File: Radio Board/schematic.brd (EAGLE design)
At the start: 55 x 70.2 mm, 8 parts, among them J1 132134RP

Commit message: added a 100uF cap
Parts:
- added C3: 08054W107MAT2A, 08054W107MAT2A:CAPC2012X94N
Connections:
- net 3V3.2: now also C3.2
- net GND: now also C3.1
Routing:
- net 3V3.2: track 36.2 -> 37.5 mm
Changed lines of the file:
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@@
 <attribute name="VALUE" x="11.049" y="13.081" size="1.27" layer="27" align="center"/>
+</element>
+<element name="C3" library="08054W107MAT2A" package="CAPC2012X94N" value="08054W107MAT2A" x="40.64" y="40.64" smashed="yes" rot="R180">
+<attribute name="DESCRIPTION" value="Multilayer Ceramic Capacitors MLCC - SMD/SMT 4V 100uF X6S 805 20%" x="40.64" y="40.64" size="1.778" layer="27" rot="R180" display="off"/>
+<attribute name="HEIGHT" value="0.94mm" x="40.64" y="40.64" size="1.778" layer="27" rot="R180" display="off"/>
+<attribute name="MANUFACTURER_NAME" value="Kyocera AVX" x="40.64" y="40.64" size="1.778" layer="27" rot="R180" display="off"/>
+<attribute name="MANUFACTURER_PART_NUMBER" value="08054W107MAT2A" x="40.64" y="40.64" size="1.778" layer="27" rot="R180" display="off"/>
+<attribute name="MOUSER_PART_NUMBER" value="581-08054W107MAT2A" x="40.64" y="40.64" size="1.778" layer="27" rot="R180" display="off"/>
+<attribute name="MOUSER_PRICE-STOCK" value="https://www.mouser.co.uk/ProductDetail/KYOCERA-AVX/08054W107MAT2A?qs=Znm5pLBrcAJdyP%2Fr3h4OXQ%3D%3D" x="40.64" y="40.64" size="1.778" layer="27" rot="R180" display="off"/>
+<attribute name="NAME" x="40.64" y="39" size="1.27" layer="25" rot="R180" align="center"/>
 </element>
 </elements>
@@
 <vertex x="0" y="0"/>
 </polygon>
-<wire x1="28.944" y1="44.207" x2="28.044" y2="44.207" width="0" layer="19" extent="1-1"/>
+<contactref element="C3" pad="1"/>
+<wire x1="35.04" y1="60.335" x2="35.04" y2="64.335" width="0" layer="19" extent="1-1"/>
+<wire x1="40.22" y1="46" x2="35.04" y2="60.335" width="0" layer="19" extent="1-1"/>
+<wire x1="40.22" y1="43.18" x2="40.22" y2="46" width="0" layer="19" extent="1-1"/>
+<wire x1="41.45" y1="40.64" x2="40.22" y2="43.18" width="0" layer="19" extent="1-1"/>
+<wire x1="35.04" y1="40.335" x2="40.22" y2="43.18" width="0" layer="19" extent="1-1"/>
+<wire x1="29.844" y1="42.407" x2="35.04" y2="40.335" width="0" layer="19" extent="1-1"/>
+<wire x1="29.844" y1="43.307" x2="29.844" y2="42.407" width="0" layer="19" extent="1-1"/>
+<wire x1="28.944" y1="43.307" x2="29.844" y2="43.307" width="0" layer="19" extent="1-1"/>
+<wire x1="28.044" y1="43.307" x2="28.944" y2="43.307" width="0" layer="19" extent="1-1"/>
+<wire x1="28.944" y1="44.207" x2="28.944" y2="43.307" width="0" layer="19" extent="1-1"/>
+<wire x1="28.044" y1="44.207" x2="28.044" y2="43.307" width="0" layer="19" extent="1-1"/>
 <wire x1="29.844" y1="44.207" x2="29.844" y2="43.307" width="0" layer="19" extent="1-1"/>
-<wire x1="29.844" y1="42.407" x2="29.844" y2="43.307" width="0" layer="19" extent="1-1"/>
-<wire x1="28.044" y1="42.407" x2="28.944" y2="42.407" width="0" layer="19" extent="1-1"/>
-<wire x1="35.04" y1="40.335" x2="29.844" y2="42.407" width="0" layer="19" extent="1-1"/>
+<wire x1="28.044" y1="42.407" x2="28.044" y2="43.307" width="0" layer="19" extent="1-1"/>
+<wire x1="28.944" y1="42.407" x2="29.844" y2="42.407" width="0" layer="19" extent="1-1"/>
+<wire x1="42" y1="25.32" x2="41.45" y2="40.64" width="0" layer="19" extent="1-1"/>
+<wire x1="48" y1="23.65" x2="42" y2="25.32" width="0" layer="19" extent="1-1"/>
+<wire x1="13.22" y1="38.335" x2="28.044" y2="42.407" width="0" layer="19" extent="1-1"/>
+<wire x1="13.22" y1="64.335" x2="35.04" y2="64.335" width="0" layer="19" extent="1-1"/>
+<wire x1="13.589" y1="9.271" x2="13.22" y2="38.335" width="0" layer="19" extent="1-1"/>
+<wire x1="8.509" y1="9.271" x2="13.589" y2="9.271" width="0" layer="19" extent="1-1"/>
+<wire x1="13.589" y1="4.191" x2="13.589" y2="9.271" width="0" layer="19" extent="1-1"/>
+<wire x1="8.509" y1="4.191" x2="8.509" y2="9.271" width="0" layer="19" extent="1-1"/>
 </signal>
 <signal name="3V3.1">
@@
 <wire x1="38.52" y1="43.18" x2="37.675" y2="42.335" width="0.3048" layer="1"/>
 <wire x1="37.675" y1="42.335" x2="35.04" y2="42.335" width="0.3048" layer="1"/>
-<wire x1="38.52" y1="43.18" x2="38.52" y2="36.41" width="0.3048" layer="1"/>
+<wire x1="38.52" y1="43.18" x2="38.52" y2="40.64" width="0.3048" layer="1"/>
+<wire x1="38.52" y1="40.64" x2="38.52" y2="36.41" width="0.3048" layer="1"/>
 <wire x1="38.52" y1="36.41" x2="39.37" y2="35.56" width="0.3048" layer="1"/>
 <via x="39.37" y="35.56" extent="1-16" drill="0.35"/>
 <wire x1="39.37" y1="35.56" x2="39.37" y2="25.41" width="0.3048" layer="16"/>
 <wire x1="39.37" y1="25.41" x2="42" y2="22.78" width="0.3048" layer="16"/>
+<contactref element="C3" pad="2"/>
+<wire x1="39.83" y1="40.64" x2="38.52" y2="40.64" width="0.3048" layer="1"/>
 </signal>
 <signal name="LIPO">

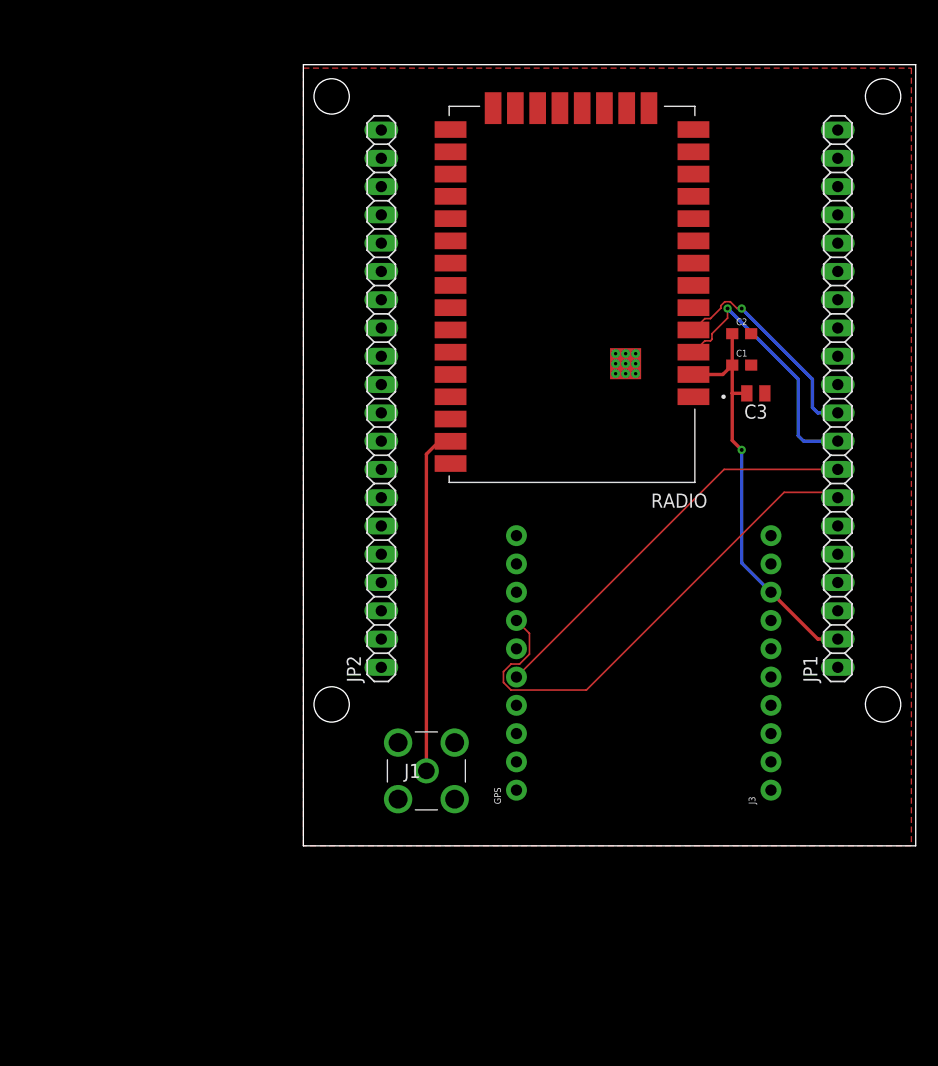
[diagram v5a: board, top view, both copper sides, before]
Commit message: updated radio
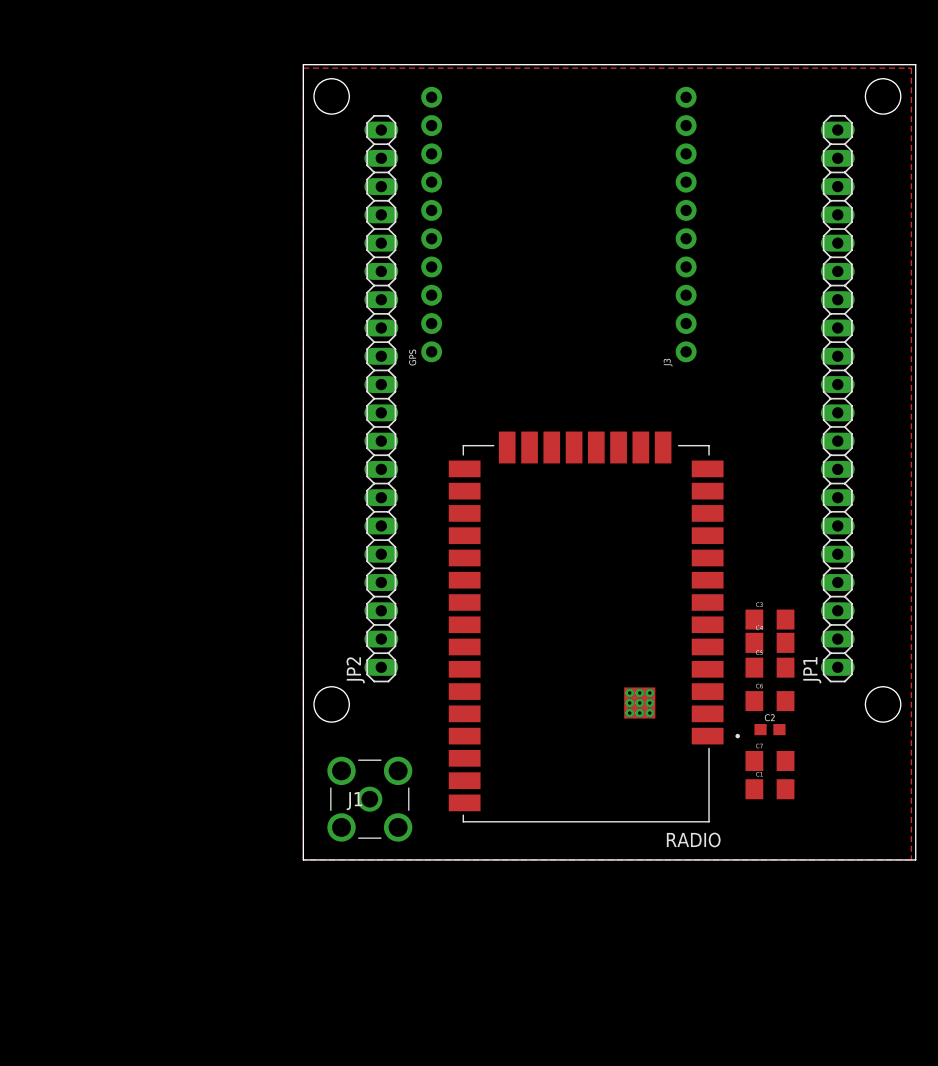
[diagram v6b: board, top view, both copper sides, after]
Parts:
- added C4, C5: 47uF, SparkFun-Retired:1206
- added C6, C7: 100uF, SparkFun-Retired:1206
- C1: device SparkFun-Capacitors:0603 -> SparkFun-Retired:1206
- C3: value 08054W107MAT2A -> 1uF; device 08054W107MAT2A:CAPC2012X94N -> SparkFun-Retired:1206
- moved GPS 40.1 mm to (11.5, 44.4)
- moved J3 40.1 mm to (34.4, 44.4)
- moved C1 38.2 mm to (41.9, 5.08)
- moved C2 35.7 mm to (41.9, 10.4)
- moved RADIO 30.5 mm to (25.4, 19.1)
- moved C3 20.4 mm to (41.9, 20.3), turned to 0 degrees
- moved J1 5.68 mm to (5.97, 4.19)
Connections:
- net 3V3.2: now also C3.1, C4.1, C5.1, C6.1, C7.1; no longer C3.2
- net GND: now also C3.2, C4.2, C5.2, C6.2, C7.2; no longer C3.1
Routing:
- net RX1: track 45.3 -> 0.68 mm
- net 3V3.2: track 37.5 -> 0.00 mm, vias 1 -> 0
- net TX1: track 36.6 -> 0.00 mm
- net RF: track 30.8 -> 0.00 mm
- net RX2: track 24.0 -> 0.68 mm, vias 1 -> 0
- net TX2: track 20.4 -> 0.68 mm, vias 1 -> 0
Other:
- board size 55 x 70.2 mm -> 55 x 71.4 mm

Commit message: Radio Board - Routed traces, missing ground plane
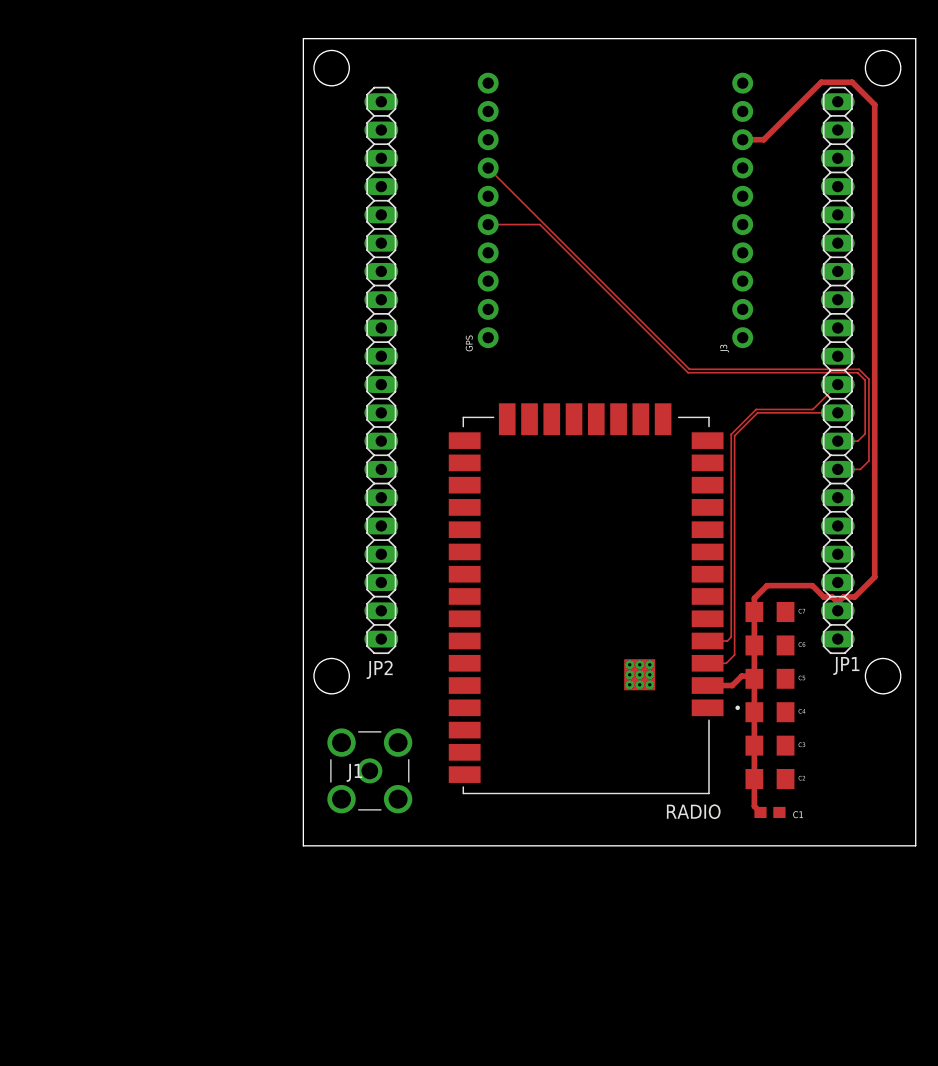
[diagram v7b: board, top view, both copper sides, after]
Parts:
- C1: value 1uF -> 100pF; device SparkFun-Retired:1206 -> SparkFun-Capacitors:0603
- C2: value 100pF -> 1uF; device SparkFun-Capacitors:0603 -> SparkFun-Retired:1206
- moved C7 13.4 mm to (41.9, 21.0)
- moved C3 11.3 mm to (41.9, 9.00)
- moved C4 6.23 mm to (41.9, 12.0)
- moved GPS 5.24 mm to (16.6, 45.6)
- moved J3 5.24 mm to (39.5, 45.6)
- moved C6 5.00 mm to (41.9, 18.0)
- moved C2 4.44 mm to (41.9, 6.00)
- moved JP1 2.54 mm to (48.0, 42.7)
- moved JP2 2.54 mm to (7.00, 42.7)
- moved J1 2.54 mm to (5.97, 6.73)
- moved RADIO 2.54 mm to (25.4, 21.6)
- moved C1 2.08 mm to (41.9, 3.00)
- moved C5 1.00 mm to (41.9, 15.0)
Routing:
- net 3V3.2: track 0.00 -> 111.1 mm
- net RX1: track 0.68 -> 52.5 mm
- net TX1: track 0.00 -> 47.2 mm
- net RX2: track 0.68 -> 32.5 mm
- net TX2: track 0.68 -> 31.9 mm
- removed copper zone on layer 1, net GND
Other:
- board size 55 x 71.4 mm -> 55 x 72.5 mm

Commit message: Planes included, added backups to gitignore
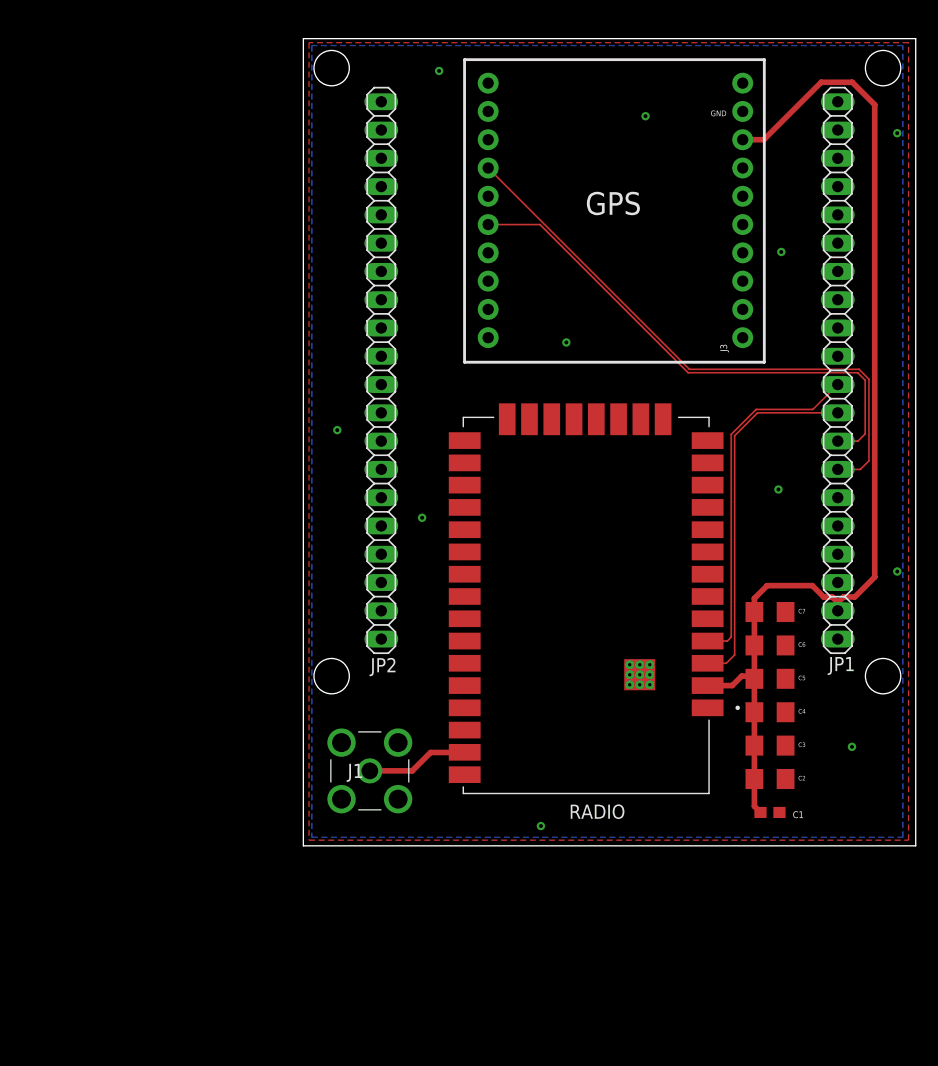
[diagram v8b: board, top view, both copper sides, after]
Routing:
- net RF: track 0.00 -> 9.70 mm
- added copper zone on layer 1, net GND
- added copper zone on layer 16, net GND
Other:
- board text added: "GND"
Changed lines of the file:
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@@
 <dimension x1="55" y1="72.7" x2="0" y2="72.7" x3="27.5" y3="77.47" textsize="1.778" layer="1"/>
 <dimension x1="55" y1="0" x2="55" y2="72.5" x3="63.5" y3="36.25" textsize="1.778" layer="1"/>
+<text x="36.576" y="65.532" size="0.508" layer="21">GND</text>
+<wire x1="14.478" y1="70.612" x2="14.478" y2="43.434" width="0.254" layer="21"/>
+<wire x1="14.478" y1="43.434" x2="41.402" y2="43.434" width="0.254" layer="21"/>
+<wire x1="41.402" y1="43.434" x2="41.402" y2="70.612" width="0.254" layer="21"/>
+<wire x1="41.402" y1="70.612" x2="14.478" y2="70.612" width="0.254" layer="21"/>
 </plain>
 <attributes>
@@
 <elements>
 <element name="JP1" library="adafruit" library_urn="urn:adsk.eagle:library:420" package="1X20" package3d_urn="urn:adsk.eagle:package:6240777/1" value="" x="48" y="42.7" smashed="yes" rot="R90">
-<attribute name="NAME" x="50.0862" y="16.9612" size="1.27" layer="25" ratio="10" rot="R180"/>
+<attribute name="NAME" x="49.5782" y="16.9612" size="1.27" layer="25" ratio="10" rot="R180"/>
 <attribute name="VALUE" x="51.175" y="17.3" size="1.27" layer="27" rot="R90"/>
 </element>
 <element name="JP2" library="adafruit" library_urn="urn:adsk.eagle:library:420" package="1X20" package3d_urn="urn:adsk.eagle:package:6240777/1" value="" x="7" y="42.7" smashed="yes" rot="R90">
-<attribute name="NAME" x="8.1762" y="16.6012" size="1.27" layer="25" ratio="10" rot="R180"/>
+<attribute name="NAME" x="8.4302" y="16.8552" size="1.27" layer="25" ratio="10" rot="R180"/>
 <attribute name="VALUE" x="10.175" y="17.3" size="1.27" layer="27" rot="R90"/>
 </element>
 <element name="GPS" library="SparkFun-Connectors" package="1X10_NO_SILK" value="" x="16.6" y="45.64" smashed="yes" rot="R90">
-<attribute name="NAME" x="15.203" y="44.37" size="0.6096" layer="25" font="vector" ratio="20" rot="R90"/>
+<attribute name="NAME" x="25.32" y="56.679" size="2.032" layer="25" ratio="20"/>
 <attribute name="VALUE" x="18.632" y="44.37" size="0.6096" layer="27" font="vector" ratio="20" rot="R90"/>
 </element>
@@
 <attribute name="MF" value="Digi International" x="52.07" y="-19.05" size="1.778" layer="27" rot="R180" display="off"/>
 <attribute name="MP" value="XBP9X-DMRS-001" x="52.07" y="-19.05" size="1.778" layer="27" rot="R180" display="off"/>
-<attribute name="NAME" x="37.56" y="3.7" size="1.27" layer="25" rot="R180"/>
+<attribute name="NAME" x="28.924" y="3.7" size="1.27" layer="25" rot="R180"/>
 <attribute name="PACKAGE" value="Module Digi International" x="52.07" y="-19.05" size="1.778" layer="27" rot="R180" display="off"/>
 <attribute name="PRICE" value="None" x="52.07" y="-19.05" size="1.778" layer="27" rot="R180" display="off"/>
 <attribute name="PURCHASE-URL" value="https://pricing.snapeda.com/search/part/XBP9X-DMRS-001/?ref=eda" x="52.07" y="-19.05" size="1.778" layer="27" rot="R180" display="off"/>
-<attribute name="VALUE" x="37.81" y="40.4" size="1.27" layer="27" rot="R180" align="top-left"/>
+<attribute name="VALUE" x="32.984" y="40.908" size="1.27" layer="27" rot="R180" align="top-left"/>
 </element>
 <element name="J1" library="132134RP" package="132134RP" value="132134RP" x="5.969" y="6.731" smashed="yes">
@@
 <attribute name="MOUSER_PRICE-STOCK" value="https://www.mouser.co.uk/ProductDetail/Amphenol-RF/132134RP?qs=Ld4zsxSTIA6y6Ienrae61w%3D%3D" x="-20.701" y="46.101" size="1.778" layer="27" display="off"/>
 <attribute name="NAME" x="4.699" y="6.731" size="1.27" layer="25" align="center"/>
-<attribute name="VALUE" x="5.969" y="13.081" size="1.27" layer="27" align="center"/>
+<attribute name="VALUE" x="6.223" y="12.319" size="1.27" layer="27" align="center"/>
 </element>
 <element name="C3" library="SparkFun-Retired" package="1206" value="1uF" x="41.91" y="9" smashed="yes">
@@
 <contactref element="C6" pad="2"/>
 <contactref element="C2" pad="2"/>
-<wire x1="36.31" y1="36.395" x2="39.46" y2="65.96" width="0" layer="19" extent="1-1"/>
+<via x="3.048" y="37.338" extent="1-16" drill="0.35"/>
+<via x="23.622" y="45.212" extent="1-16" drill="0.35"/>
+<via x="10.668" y="29.464" extent="1-16" drill="0.35"/>
+<via x="12.192" y="69.596" extent="1-16" drill="0.35"/>
+<via x="30.734" y="65.532" extent="1-16" drill="0.35"/>
+<via x="42.926" y="53.34" extent="1-16" drill="0.35"/>
+<via x="53.34" y="64.008" extent="1-16" drill="0.35"/>
+<via x="42.672" y="32.004" extent="1-16" drill="0.35"/>
+<via x="53.34" y="24.638" extent="1-16" drill="0.35"/>
+<via x="49.276" y="8.89" extent="1-16" drill="0.35"/>
+<via x="21.336" y="1.778" extent="1-16" drill="0.35"/>
+<polygon width="0.254" layer="1" isolate="0.635">
+<vertex x="0.508" y="72.136"/>
+<vertex x="0.508" y="0.508"/>
+<vertex x="54.356" y="0.508"/>
+<vertex x="54.356" y="72.136"/>
+</polygon>
+<polygon width="0.254" layer="16" isolate="0.635">
+<vertex x="0.762" y="71.882"/>
+<vertex x="0.762" y="0.762"/>
+<vertex x="53.848" y="0.762"/>
+<vertex x="53.848" y="71.882"/>
+</polygon>
 <wire x1="36.31" y1="32.395" x2="36.31" y2="36.395" width="0" layer="19" extent="1-1"/>
-<wire x1="48" y1="26.19" x2="36.31" y2="32.395" width="0" layer="19" extent="1-1"/>
-<wire x1="43.31" y1="21" x2="48" y2="26.19" width="0" layer="19" extent="1-1"/>
-<wire x1="43.31" y1="18" x2="43.31" y2="21" width="0" layer="19" extent="1-1"/>
-<wire x1="43.31" y1="15" x2="43.31" y2="18" width="0" layer="19" extent="1-1"/>
-<wire x1="43.31" y1="12" x2="43.31" y2="15" width="0" layer="19" extent="1-1"/>
-<wire x1="43.31" y1="9" x2="43.31" y2="12" width="0" layer="19" extent="1-1"/>
-<wire x1="43.31" y1="6" x2="43.31" y2="9" width="0" layer="19" extent="1-1"/>
-<wire x1="42.76" y1="3" x2="43.31" y2="6" width="0" layer="19" extent="1-1"/>
-<wire x1="36.31" y1="12.395" x2="43.31" y2="12" width="0" layer="19" extent="1-1"/>
-<wire x1="31.114" y1="14.467" x2="36.31" y2="12.395" width="0" layer="19" extent="1-1"/>
-<wire x1="31.114" y1="15.367" x2="31.114" y2="14.467" width="0" layer="19" extent="1-1"/>
-<wire x1="31.114" y1="16.267" x2="31.114" y2="15.367" width="0" layer="19" extent="1-1"/>
-<wire x1="30.214" y1="16.267" x2="31.114" y2="16.267" width="0" layer="19" extent="1-1"/>
-<wire x1="29.314" y1="16.267" x2="30.214" y2="16.267" width="0" layer="19" extent="1-1"/>
-<wire x1="29.314" y1="15.367" x2="29.314" y2="16.267" width="0" layer="19" extent="1-1"/>
-<wire x1="30.214" y1="15.367" x2="31.114" y2="15.367" width="0" layer="19" extent="1-1"/>
-<wire x1="29.314" y1="14.467" x2="29.314" y2="15.367" width="0" layer="19" extent="1-1"/>
-<wire x1="30.214" y1="14.467" x2="31.114" y2="14.467" width="0" layer="19" extent="1-1"/>
-<wire x1="14.49" y1="10.395" x2="29.314" y2="14.467" width="0" layer="19" extent="1-1"/>
-<wire x1="8.509" y1="9.271" x2="14.49" y2="10.395" width="0" layer="19" extent="1-1"/>
-<wire x1="3.429" y1="9.271" x2="8.509" y2="9.271" width="0" layer="19" extent="1-1"/>
-<wire x1="8.509" y1="4.191" x2="8.509" y2="9.271" width="0" layer="19" extent="1-1"/>
-<wire x1="3.429" y1="4.191" x2="3.429" y2="9.271" width="0" layer="19" extent="1-1"/>
-<wire x1="14.49" y1="36.395" x2="36.31" y2="36.395" width="0" layer="19" extent="1-1"/>
+<wire x1="42.672" y1="32.004" x2="36.31" y2="32.395" width="0" layer="19" extent="1-1"/>
 </signal>
 <signal name="3V3.1">
@@
 <contactref element="RADIO" pad="36"/>
 <contactref element="J1" pad="1"/>
-<wire x1="5.969" y1="6.731" x2="14.49" y2="8.395" width="0" layer="19" extent="1-1"/>
+<wire x1="5.969" y1="6.731" x2="9.779" y2="6.731" width="0.508" layer="1"/>
+<wire x1="11.43" y1="8.382" x2="14.986" y2="8.382" width="0.508" layer="1"/>
+<wire x1="9.779" y1="6.731" x2="11.43" y2="8.382" width="0.508" layer="1"/>
+<wire x1="14.986" y1="8.382" x2="14.49" y2="8.395" width="0" layer="19" extent="1-1"/>
 </signal>
 </signals>
